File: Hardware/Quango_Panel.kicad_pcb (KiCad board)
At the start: 2 copper layers, 76 x 128.5 mm, 30 parts

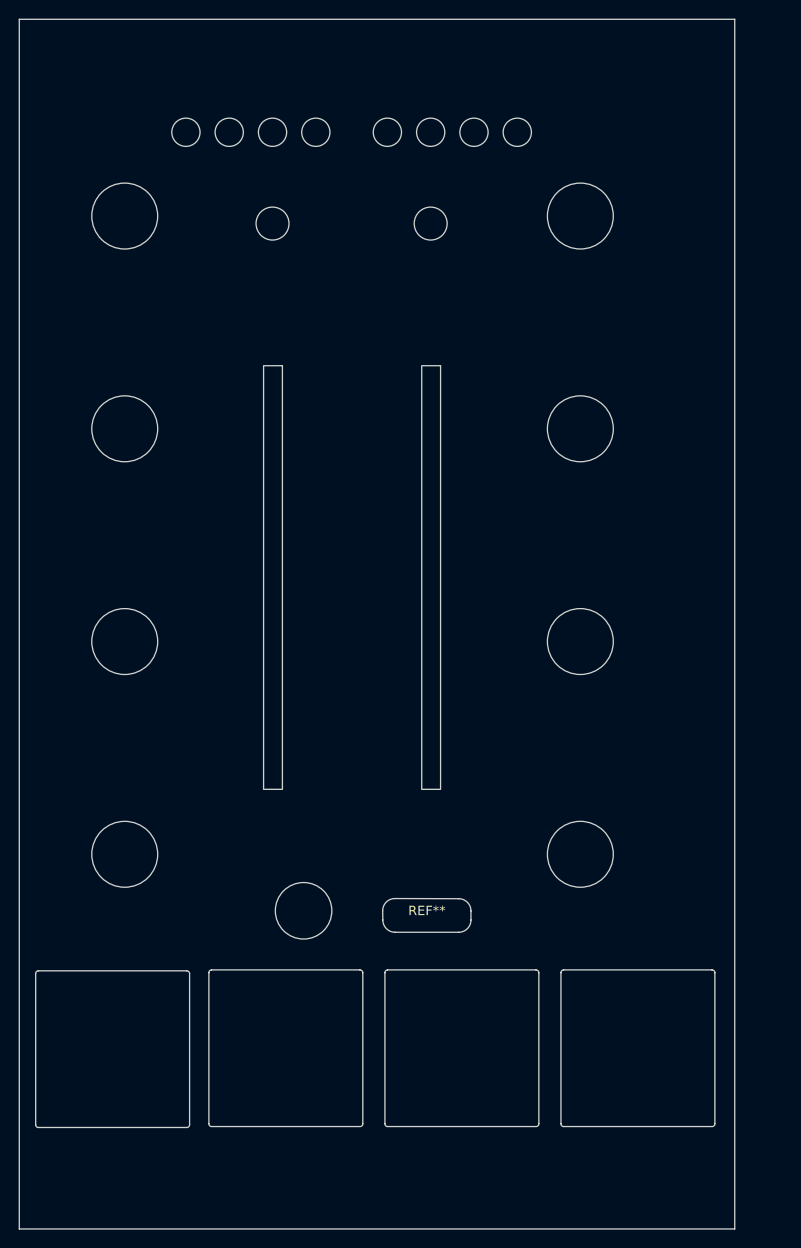
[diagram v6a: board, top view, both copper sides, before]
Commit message: Updating Controls and Panel to support gates
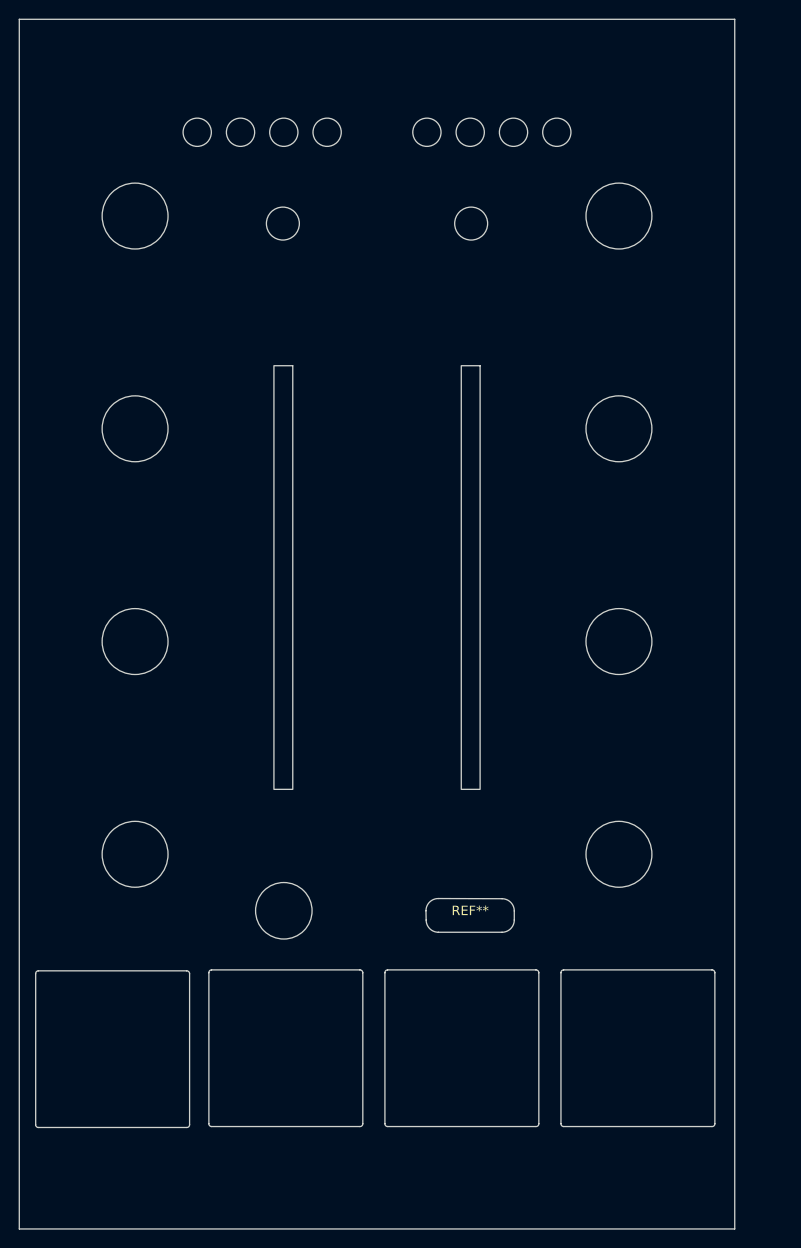
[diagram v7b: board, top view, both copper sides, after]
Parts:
- moved Ref** 5.20 mm to (118.5, 155.5)
- moved Ref** 5.20 mm to (118.5, 33.0)
- moved REF** 4.60 mm to (97.9, 125.2)
- moved RESET 4.30 mm to (98.0, 51.7)
- moved Level1 4.20 mm to (99.7, 60.0)
- moved Ref** 4.20 mm to (102.5, 42.0)
- moved Ref** 4.20 mm to (93.3, 42.0)
- moved Ref** 4.20 mm to (97.9, 42.0)
- moved Ref** 4.20 mm to (107.1, 42.0)
- moved Ref** 4.10 mm to (113.7, 50.9)
- moved Ref** 4.10 mm to (113.7, 118.7)
- moved Ref** 4.10 mm to (113.7, 96.1)
- moved Ref** 4.10 mm to (113.7, 73.5)
- moved Ref** 2.10 mm to (78.1, 124.7)
- moved Ref** 1.20 mm to (68.9, 42.0)
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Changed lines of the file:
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@@
   (net 0 "")
   (footprint "Custom_Footprints:LED_Hole_3mm" (layer "F.Cu")
-    (at 76.9 42 90)
+    (at 78.1 42 90)
     (descr "Mounting Hole 6mm, no annular")
     (tags "mounting hole 6mm no annular")
@@
   )
   (footprint "Custom_Footprints:LED_Hole_3mm" (layer "F.Cu")
-    (at 89.1 42 90)
+    (at 93.3 42 90)
     (descr "Mounting Hole 6mm, no annular")
     (tags "mounting hole 6mm no annular")
@@
   )
   (footprint "Custom_Footprints:LED_Hole_3mm" (layer "F.Cu")
-    (at 93.7 42 90)
+    (at 97.9 42 90)
     (descr "Mounting Hole 6mm, no annular")
     (tags "mounting hole 6mm no annular")
@@
   )
   (footprint "Custom_Footprints:Alpha_9mm_pot_hole" (layer "F.Cu")
-    (at 61.2 50.9)
+    (at 62.3 50.9)
     (descr "Mounting Hole 7mm")
     (tags "mounting hole 7mm")
@@
   )
   (footprint "Custom_Footprints:Oval_Mounting_Hole" locked (layer "F.Cu")
-    (at 113.3 33)
+    (at 118.5 33)
     (descr "Mounting Hole 6mm, no annular")
     (tags "mounting hole 6mm no annular")
@@
   )
   (footprint "Custom_Footprints:Alpha_9mm_pot_hole" (layer "F.Cu")
-    (at 109.6 96.1)
+    (at 113.7 96.1)
     (descr "Mounting Hole 7mm")
     (tags "mounting hole 7mm")
@@
   )
   (footprint "Custom_Footprints:Thonkiconn_Socket_MountingHole_6mm" (layer "F.Cu")
-    (at 80.2 124.7)
+    (at 78.1 124.7)
     (descr "Mounting Hole 6mm, no annular")
     (tags "mounting hole 6mm no annular")
@@
   )
   (footprint "Custom_Footprints:Alpha_9mm_pot_hole" (layer "F.Cu")
-    (at 61.2 118.7)
+    (at 62.3 118.7)
     (descr "Mounting Hole 7mm")
     (tags "mounting hole 7mm")
@@
   )
   (footprint "Custom_Footprints:Alpha_9mm_pot_hole" (layer "F.Cu")
-    (at 109.6 73.5)
+    (at 113.7 73.5)
     (descr "Mounting Hole 7mm")
     (tags "mounting hole 7mm")
@@
   )
   (footprint "Custom_Footprints:LED_Hole_3mm" (layer "F.Cu")
-    (at 67.7 42 90)
+    (at 68.9 42 90)
     (descr "Mounting Hole 6mm, no annular")
     (tags "mounting hole 6mm no annular")
@@
   )
   (footprint "Custom_Footprints:LED_Hole_3mm" (layer "F.Cu")
-    (at 98.3 42 90)
+    (at 102.5 42 90)
     (descr "Mounting Hole 6mm, no annular")
     (tags "mounting hole 6mm no annular")
@@
   )
   (footprint "Custom_Footprints:Alpha_9mm_pot_hole" (layer "F.Cu")
-    (at 109.6 50.9)
+    (at 113.7 50.9)
     (descr "Mounting Hole 7mm")
     (tags "mounting hole 7mm")
@@
   )
   (footprint "Custom_Footprints:Alpha_9mm_pot_hole" (layer "F.Cu")
-    (at 109.6 118.7)
+    (at 113.7 118.7)
     (descr "Mounting Hole 7mm")
     (tags "mounting hole 7mm")
@@
   )
   (footprint "Custom_Footprints:Oval_Mounting_Hole" locked (layer "F.Cu")
-    (at 113.3 155.5)
+    (at 118.5 155.5)
     (descr "Mounting Hole 6mm, no annular")
     (tags "mounting hole 6mm no annular")
@@
   )
   (footprint "Custom_Footprints:Alpha_9mm_pot_hole" (layer "F.Cu")
-    (at 61.2 96.1)
+    (at 62.3 96.1)
     (descr "Mounting Hole 7mm")
     (tags "mounting hole 7mm")
@@
   )
   (footprint "Custom_Footprints:USB_C_Cutout" (layer "F.Cu")
-    (at 93.3 125.2)
+    (at 97.9 125.2)
     (attr smd)
     (fp_text reference "REF**" (at 0 -0.5 unlocked) (layer "F.SilkS")
@@
   )
   (footprint "Custom_Footprints:Alpha_9mm_pot_hole" (layer "F.Cu")
-    (at 61.2 73.5)
+    (at 62.3 73.5)
     (descr "Mounting Hole 7mm")
     (tags "mounting hole 7mm")
@@
   )
   (footprint "Custom_Footprints:LED_Hole_3mm" (layer "F.Cu")
-    (at 102.9 42 90)
+    (at 107.1 42 90)
     (descr "Mounting Hole 6mm, no annular")
     (tags "mounting hole 6mm no annular")
@@
   )
   (footprint "Custom_Footprints:Potentiometer_Bourns_PTA4543_Slot" (layer "F.Cu")
-    (at 78.7 60.05 -90)
+    (at 79.8 60.05 -90)
     (descr "Bourns single-gang slide potentiometer, 45.0mm travel, https://www.bourns.com/docs/Product-Datasheets/pta.pdf")
     (tags "Bourns single-gang slide potentiometer 45.0mm")
@@
   )
   (footprint "Custom_Footprints:LED_Hole_3mm" (layer "F.Cu")
-    (at 72.3 42 90)
+    (at 73.5 42 90)
     (descr "Mounting Hole 6mm, no annular")
     (tags "mounting hole 6mm no annular")
@@
   )
   (footprint "Custom_Footprints:Potentiometer_Bourns_PTA4543_Slot" (layer "F.Cu")
-    (at 95.5 60.05 -90)
+    (at 99.7 60.05 -90)
     (descr "Bourns single-gang slide potentiometer, 45.0mm travel, https://www.bourns.com/docs/Product-Datasheets/pta.pdf")
     (tags "Bourns single-gang slide potentiometer 45.0mm")
@@
   )
   (footprint "Custom_Footprints:LED_Hole_3mm" (layer "F.Cu")
-    (at 81.5 42 90)
+    (at 82.7 42 90)
     (descr "Mounting Hole 6mm, no annular")
     (tags "mounting hole 6mm no annular")
@@
   )
   (footprint "Custom_Footprints:Small_Pushbutton_Hole_3.5mm" (layer "B.Cu")
-    (at 76.9 51.7)
+    (at 78 51.7)
     (descr "Button Hole 3.5mm")
     (attr through_hole)
@@
   )
   (footprint "Custom_Footprints:Small_Pushbutton_Hole_3.5mm" (layer "B.Cu")
-    (at 93.7 51.7)
+    (at 98 51.7)
     (descr "Button Hole 3.5mm")
     (attr through_hole)
@@
     )
   )
-  (gr_rect locked (start 50.1 39) (end 120.7 149) (layer "Dwgs.User") (width 0.15) (fill none))
-  (gr_line locked (start 85.4 29) (end 85.4 160.6) (layer "Dwgs.User") (width 0.15))
+  (gr_rect locked (start 50.1 39) (end 125.9 149) (layer "Dwgs.User") (width 0.15) (fill none))
+  (gr_line locked (start 88 29) (end 88 160.6) (layer "Dwgs.User") (width 0.15))
   (gr_rect locked (start 50 30) (end 126 158.5) (layer "Edge.Cuts") (width 0.1) (fill none))
 )

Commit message: Increased size to 16HP
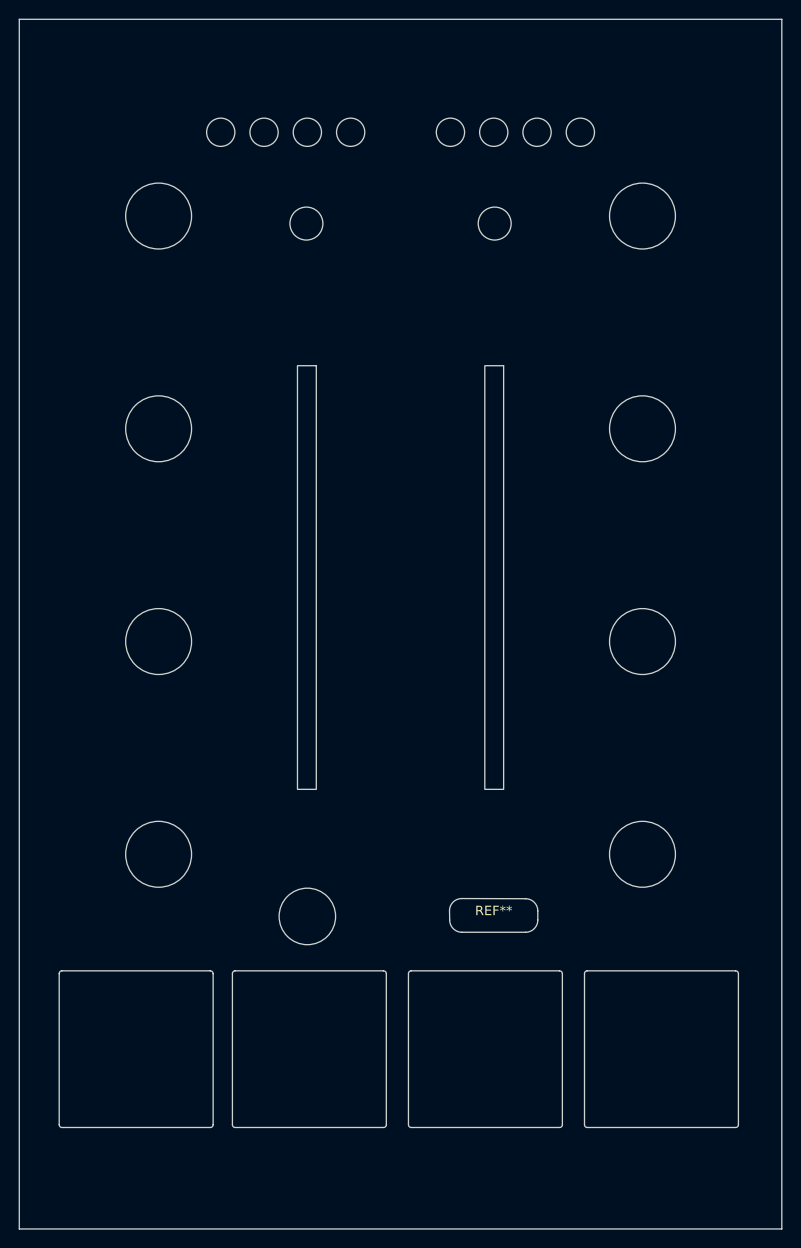
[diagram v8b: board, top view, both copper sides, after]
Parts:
- moved Ref** 5.00 mm to (123.5, 155.5)
- moved Ref** 5.00 mm to (123.5, 33.0)
- moved Ref** 2.57 mm to (80.6, 125.3)
- moved REF** 2.50 mm to (99.5, 139.4)
- moved REF** 2.50 mm to (118.2, 139.4)
- moved REF** 2.50 mm to (80.8, 139.4)
- moved Level1 2.50 mm to (82.3, 60.0)
- moved Level1 2.50 mm to (102.2, 60.0)
- moved REF** 2.50 mm to (62.4, 139.4)
- moved REF** 2.50 mm to (100.4, 125.2)
- moved RESET 2.50 mm to (80.5, 51.7)
- moved RESET 2.50 mm to (100.5, 51.7)
- moved Ref** 2.50 mm to (80.6, 42.0)
- moved Ref** 2.50 mm to (71.4, 42.0)
- moved Ref** 2.50 mm to (105.0, 42.0)
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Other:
- board size 76 x 128.5 mm -> 81 x 128.5 mm
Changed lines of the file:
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@@
   (net 0 "")
   (footprint "Custom_Footprints:LED_Hole_3mm" (layer "F.Cu")
-    (at 78.1 42 90)
+    (at 80.6 42 90)
     (descr "Mounting Hole 6mm, no annular")
     (tags "mounting hole 6mm no annular")
@@
   )
   (footprint "Custom_Footprints:RJ45_Molex_42878-8506_Mounting_Hole" (layer "F.Cu")
-    (at 59.9 139.4)
+    (at 62.4 139.4)
     (descr "RJ45 vertical connector https://www.on-shore.com/wp-content/uploads/PJ012-8P8CX.pdf")
     (tags "RJ45 PJ012")
@@
   )
   (footprint "Custom_Footprints:RJ45_Molex_42878-8506_Mounting_Hole" (layer "F.Cu")
-    (at 97 139.3)
+    (at 99.5 139.4)
     (descr "RJ45 vertical connector https://www.on-shore.com/wp-content/uploads/PJ012-8P8CX.pdf")
     (tags "RJ45 PJ012")
@@
   )
   (footprint "Custom_Footprints:LED_Hole_3mm" (layer "F.Cu")
-    (at 93.3 42 90)
+    (at 95.8 42 90)
     (descr "Mounting Hole 6mm, no annular")
     (tags "mounting hole 6mm no annular")
@@
   )
   (footprint "Custom_Footprints:LED_Hole_3mm" (layer "F.Cu")
-    (at 97.9 42 90)
+    (at 100.4 42 90)
     (descr "Mounting Hole 6mm, no annular")
     (tags "mounting hole 6mm no annular")
@@
   )
   (footprint "Custom_Footprints:Alpha_9mm_pot_hole" (layer "F.Cu")
-    (at 62.3 50.9)
+    (at 64.8 50.9)
     (descr "Mounting Hole 7mm")
     (tags "mounting hole 7mm")
@@
   )
   (footprint "Custom_Footprints:Oval_Mounting_Hole" locked (layer "F.Cu")
-    (at 118.5 33)
+    (at 123.5 33)
     (descr "Mounting Hole 6mm, no annular")
     (tags "mounting hole 6mm no annular")
@@
   )
   (footprint "Custom_Footprints:Alpha_9mm_pot_hole" (layer "F.Cu")
-    (at 113.7 96.1)
+    (at 116.2 96.1)
     (descr "Mounting Hole 7mm")
     (tags "mounting hole 7mm")
@@
   )
   (footprint "Custom_Footprints:Thonkiconn_Socket_MountingHole_6mm" (layer "F.Cu")
-    (at 78.1 124.7)
+    (at 80.6 125.3)
     (descr "Mounting Hole 6mm, no annular")
     (tags "mounting hole 6mm no annular")
@@
   )
   (footprint "Custom_Footprints:Alpha_9mm_pot_hole" (layer "F.Cu")
-    (at 62.3 118.7)
+    (at 64.8 118.7)
     (descr "Mounting Hole 7mm")
     (tags "mounting hole 7mm")
@@
   )
   (footprint "Custom_Footprints:Alpha_9mm_pot_hole" (layer "F.Cu")
-    (at 113.7 73.5)
+    (at 116.2 73.5)
     (descr "Mounting Hole 7mm")
     (tags "mounting hole 7mm")
@@
   )
   (footprint "Custom_Footprints:LED_Hole_3mm" (layer "F.Cu")
-    (at 68.9 42 90)
+    (at 71.4 42 90)
     (descr "Mounting Hole 6mm, no annular")
     (tags "mounting hole 6mm no annular")
@@
   )
   (footprint "Custom_Footprints:LED_Hole_3mm" (layer "F.Cu")
-    (at 102.5 42 90)
+    (at 105 42 90)
     (descr "Mounting Hole 6mm, no annular")
     (tags "mounting hole 6mm no annular")
@@
   )
   (footprint "Custom_Footprints:Alpha_9mm_pot_hole" (layer "F.Cu")
-    (at 113.7 50.9)
+    (at 116.2 50.9)
     (descr "Mounting Hole 7mm")
     (tags "mounting hole 7mm")
@@
   )
   (footprint "Custom_Footprints:Alpha_9mm_pot_hole" (layer "F.Cu")
-    (at 113.7 118.7)
+    (at 116.2 118.7)
     (descr "Mounting Hole 7mm")
     (tags "mounting hole 7mm")
@@
   )
   (footprint "Custom_Footprints:Oval_Mounting_Hole" locked (layer "F.Cu")
-    (at 118.5 155.5)
+    (at 123.5 155.5)
     (descr "Mounting Hole 6mm, no annular")
     (tags "mounting hole 6mm no annular")
@@
   )
   (footprint "Custom_Footprints:Alpha_9mm_pot_hole" (layer "F.Cu")
-    (at 62.3 96.1)
+    (at 64.8 96.1)
     (descr "Mounting Hole 7mm")
     (tags "mounting hole 7mm")
@@
   )
   (footprint "Custom_Footprints:USB_C_Cutout" (layer "F.Cu")
-    (at 97.9 125.2)
+    (at 100.4 125.2)
     (attr smd)
     (fp_text reference "REF**" (at 0 -0.5 unlocked) (layer "F.SilkS")
@@
   )
   (footprint "Custom_Footprints:RJ45_Molex_42878-8506_Mounting_Hole" (layer "F.Cu")
-    (at 115.7 139.3)
+    (at 118.2 139.4)
     (descr "RJ45 vertical connector https://www.on-shore.com/wp-content/uploads/PJ012-8P8CX.pdf")
     (tags "RJ45 PJ012")
@@
   )
   (footprint "Custom_Footprints:Alpha_9mm_pot_hole" (layer "F.Cu")
-    (at 62.3 73.5)
+    (at 64.8 73.5)
     (descr "Mounting Hole 7mm")
     (tags "mounting hole 7mm")
@@
   )
   (footprint "Custom_Footprints:LED_Hole_3mm" (layer "F.Cu")
-    (at 107.1 42 90)
+    (at 109.6 42 90)
     (descr "Mounting Hole 6mm, no annular")
     (tags "mounting hole 6mm no annular")
@@
   )
   (footprint "Custom_Footprints:Potentiometer_Bourns_PTA4543_Slot" (layer "F.Cu")
-    (at 79.8 60.05 -90)
+    (at 82.3 60.05 -90)
     (descr "Bourns single-gang slide potentiometer, 45.0mm travel, https://www.bourns.com/docs/Product-Datasheets/pta.pdf")
     (tags "Bourns single-gang slide potentiometer 45.0mm")
@@
   )
   (footprint "Custom_Footprints:LED_Hole_3mm" (layer "F.Cu")
-    (at 73.5 42 90)
+    (at 76 42 90)
     (descr "Mounting Hole 6mm, no annular")
     (tags "mounting hole 6mm no annular")
@@
   )
   (footprint "Custom_Footprints:Potentiometer_Bourns_PTA4543_Slot" (layer "F.Cu")
-    (at 99.7 60.05 -90)
+    (at 102.2 60.05 -90)
     (descr "Bourns single-gang slide potentiometer, 45.0mm travel, https://www.bourns.com/docs/Product-Datasheets/pta.pdf")
     (tags "Bourns single-gang slide potentiometer 45.0mm")
@@
   )
   (footprint "Custom_Footprints:LED_Hole_3mm" (layer "F.Cu")
-    (at 82.7 42 90)
+    (at 85.2 42 90)
     (descr "Mounting Hole 6mm, no annular")
     (tags "mounting hole 6mm no annular")
@@
   )
   (footprint "Custom_Footprints:RJ45_Molex_42878-8506_Mounting_Hole" (layer "F.Cu")
-    (at 78.3 139.3)
+    (at 80.8 139.4)
     (descr "RJ45 vertical connector https://www.on-shore.com/wp-content/uploads/PJ012-8P8CX.pdf")
     (tags "RJ45 PJ012")
@@
   )
   (footprint "Custom_Footprints:Small_Pushbutton_Hole_3.5mm" (layer "B.Cu")
-    (at 78 51.7)
+    (at 80.5 51.7)
     (descr "Button Hole 3.5mm")
     (attr through_hole)
@@
   )
   (footprint "Custom_Footprints:Small_Pushbutton_Hole_3.5mm" (layer "B.Cu")
-    (at 98 51.7)
+    (at 100.5 51.7)
     (descr "Button Hole 3.5mm")
     (attr through_hole)
@@
     )
   )
-  (gr_rect locked (start 50.1 39) (end 125.9 149) (layer "Dwgs.User") (width 0.15) (fill none))
-  (gr_line locked (start 88 29) (end 88 160.6) (layer "Dwgs.User") (width 0.15))
-  (gr_rect locked (start 50 30) (end 126 158.5) (layer "Edge.Cuts") (width 0.1) (fill none))
+  (gr_line locked (start 90.5 27.7) (end 90.5 32.1) (layer "Dwgs.User") (width 0.15))
+  (gr_rect locked (start 50.1 39) (end 130.9 149) (layer "Dwgs.User") (width 0.15) (fill none))
+  (gr_line locked (start 90.5 29) (end 90.5 160.6) (layer "Dwgs.User") (width 0.15))
+  (gr_rect locked (start 50 30) (end 131 158.5) (layer "Edge.Cuts") (width 0.1) (fill none))
 )
